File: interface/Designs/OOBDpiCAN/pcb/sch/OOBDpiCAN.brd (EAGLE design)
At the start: 65 x 56 mm, 73 parts, among them Q1 16MHz, X1 RASPI_BOARD_B+_H

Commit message: add USB-HUB GL850G lbr
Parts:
- added U$14: GL850G-31, pimoroni:TSSOP28
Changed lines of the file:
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@@
 <element name="R6" library="resistor" package="R0603" value="120R" x="-49.53" y="50.8"/>
 <element name="X1" library="raspberrypi_bastelstube_v13" package="RASPI_BOARD_B+HAT" value="RASPI_BOARD_B+_H" x="0" y="0"/>
+<element name="U$14" library="pimoroni" package="TSSOP28" value="GL850G-31" x="-78.74" y="5.08"/>
 </elements>
 <signals>

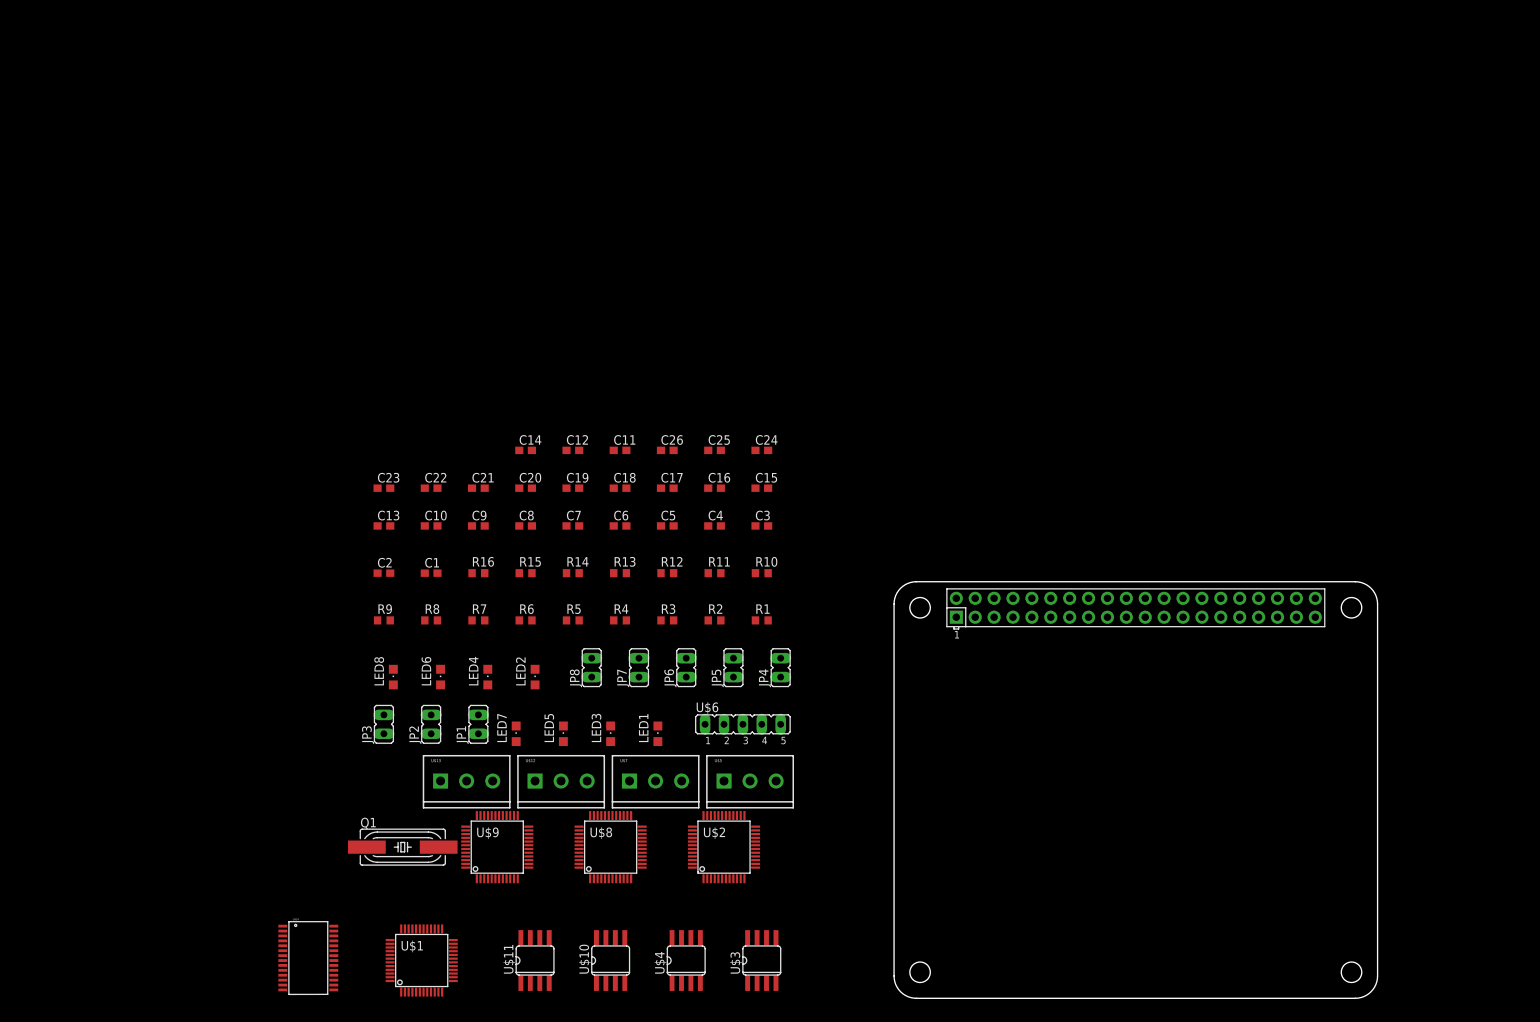
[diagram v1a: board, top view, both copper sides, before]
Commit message: 4Port USB Hub GL850G connected add ISO1050 alternative CAN interfaces
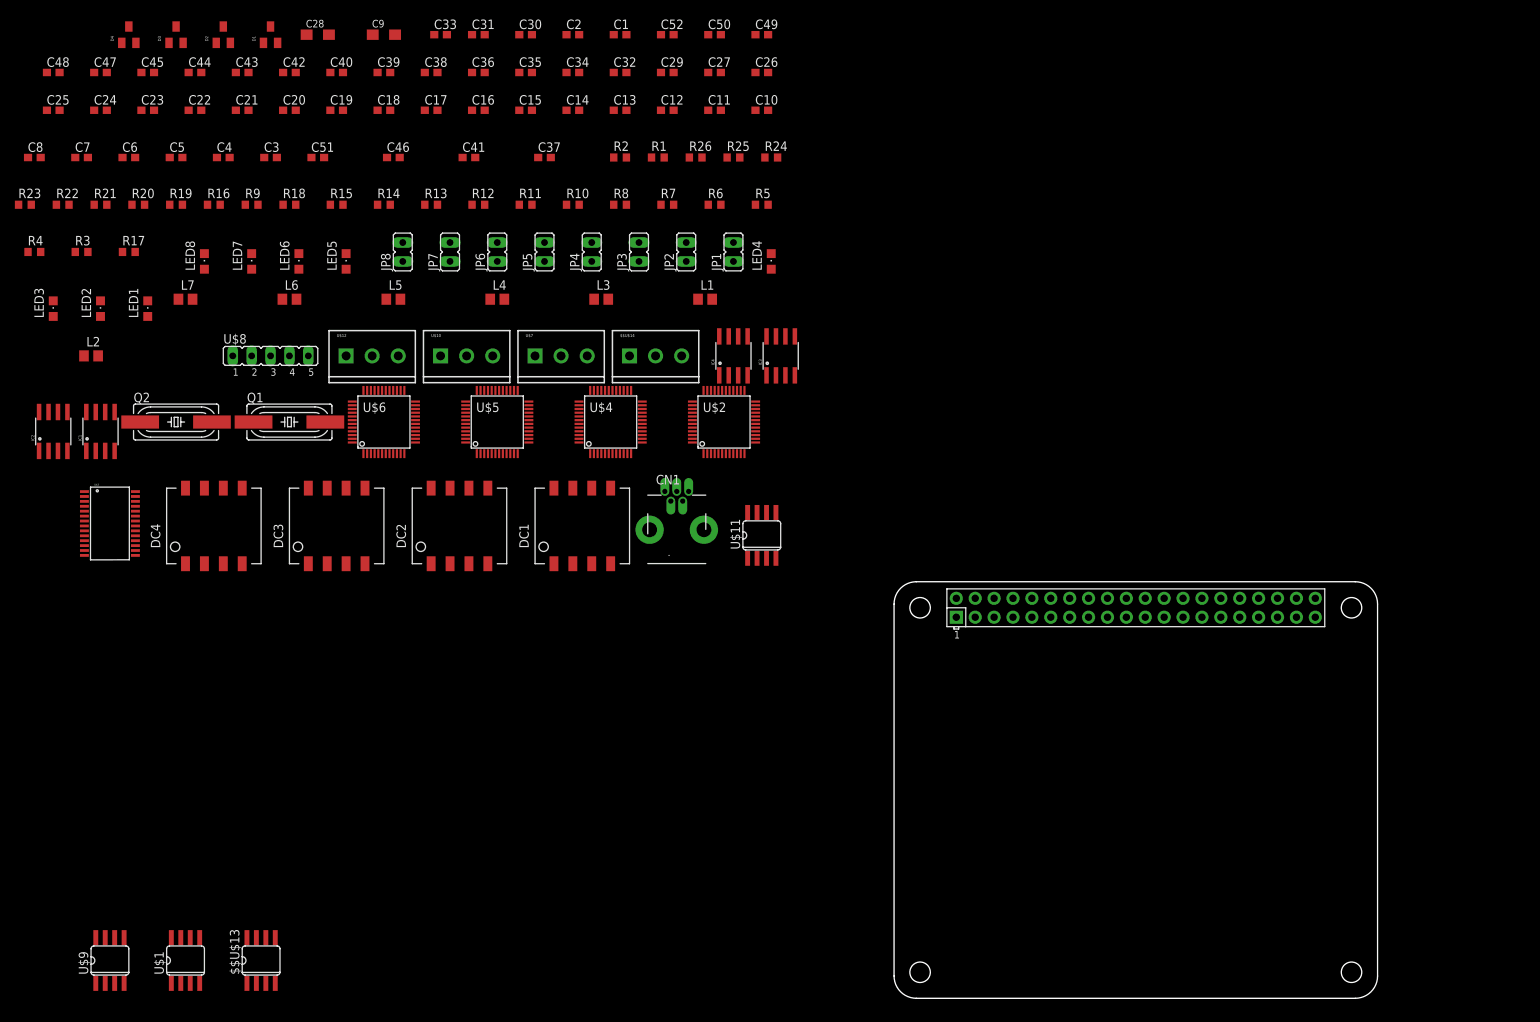
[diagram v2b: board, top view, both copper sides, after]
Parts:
- removed U$13: (no value), SparkFun-Connectors:SCREWTERMINAL-3.5MM-3
- removed U$14: GL850G-31, pimoroni:TSSOP28
- added $$U$13: MCP2551SO8, can:SO08
- added $$U$14: (no value), SparkFun-Connectors:SCREWTERMINAL-3.5MM-3
- added C27, C29, C32, C34, C35, C36, C38, C39, C40, C42, C43, C44, C45, C47, C48, C49, C50, C52: 100nF, resistor:C0603
- added C28: 22uF/6.3V, rcl:SMC_A
- added C30, C31: 18pF, resistor:C0603
- added C33: 1uF, resistor:C0603
- added C37, C41, C46, C51: NA(10nF), resistor:C0603
- added CN1: (no value), adafruit:USB-MINIB-THM-MOLEX
- added D1, D2, D3, D4: PESD1CAN, Industrialberry:SOT23
- added DC1, DC2, DC3, DC4: (no value), Industrialberry:R1SE
- added IC1, IC2, IC3, IC4: (no value), Industrialberry:SO-08
- added L1, L3, L4, L5, L6, L7: 2508056017Y2, rcl:L0805
- added L2: NA(2508056017Y2), rcl:L0805
- added Q2: 16MHz, crystal:SM49
- added R17: NA(47k), resistor:R0603
- added R18: 680R, resistor:R0603
- added R19: 10k, resistor:R0603
- added R20, R21, R22, R23, R24, R25, R26: 60R, resistor:R0603
- C1, C2: value 100nF -> 33pF
- C11, C12, C14: value 18pF -> 100nF
- C9: value 100nF -> 22uF/6.3V; device resistor:C0603 -> rcl:SMC_A
- LED2, LED4: value green -> yellow
- LED5, LED7: value yellow -> green
- Q1: value 16MHz -> 12MHz
- R1, R2: value 510R -> 10k
- R11, R3, R4: value 120R -> 510R
- R16: value 120R -> 10k
- R9: value 510R -> 60R
- U$1, U$9: value STM32F042CT -> MCP2551SO8; device micro-stm_v3:LQFP48 -> can:SO08
- U$10: value MCP2551SO8 -> (none); device can:SO08 -> SparkFun-Connectors:SCREWTERMINAL-3.5MM-3
- U$3: value MCP2551SO8 -> GL850G-31; device can:SO08 -> pimoroni:TSSOP28
- U$4: value MCP2551SO8 -> STM32F042CT; device can:SO08 -> micro-stm_v3:LQFP48
- U$5: value (none) -> STM32F042CT; device SparkFun-Connectors:SCREWTERMINAL-3.5MM-3 -> micro-stm_v3:LQFP48
- U$6: value (none) -> STM32F042CT; device jumper:JP5 -> micro-stm_v3:LQFP48
- U$8: value STM32F042CT -> (none); device micro-stm_v3:LQFP48 -> jumper:JP5
- moved U$3 105.3 mm to (-105.4, 63.5)
- moved C24 100.0 mm to (-106.7, 119.4)
- moved C25 100.0 mm to (-113.0, 119.4)
- moved LED3 94.2 mm to (-113.0, 92.7)
- moved R3 93.0 mm to (-109.2, 100.3)
- moved R4 93.0 mm to (-115.6, 100.3)
- moved LED1 89.3 mm to (-100.3, 92.7)
- moved U$10 84.4 mm to (-61.0, 86.4)
- moved U$8 83.1 mm to (-90.2, 85.1)
- moved C4 82.6 mm to (-90.2, 113.0)
- moved C6 82.6 mm to (-102.9, 113.0)
- moved C3 82.5 mm to (-83.8, 113.0)
- moved C5 82.5 mm to (-96.5, 113.0)
- moved C7 82.5 mm to (-109.2, 113.0)
- moved C8 82.5 mm to (-115.6, 113.0)
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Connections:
- net MC0_2 renamed MCO_0
- removed net N$1: U$10.4, U$8.45
- removed net N$5: U$10.1, U$8.46
- removed net N$9 (its old number): LED6.C, R12.2
- removed net NRST3: U$2.7
- removed net SWCLK2: U$1.37, U$6.2
- removed net SWCLK3: U$2.37
- removed net SWDIO2: U$1.34, U$6.4
- removed net SWDIO3: U$2.34
- removed net USB0_DM1: U$9.32
- removed net USB0_DM2: U$1.32
- removed net USB0_DM3: U$2.32
- removed net USB0_DP1: U$9.33
- removed net USB0_DP2: U$1.33
- removed net USB0_DP3: U$2.33
- new net CAN1-H: D1.2, IC1.7, R20.1, U$1.7, U$7.2
- new net CAN1-L: D1.1, IC1.6, JP3.2, U$1.6, U$7.1
- new net CAN2-H: D3.2, IC3.7, R23.1, U$11.7, U$12.2
- new net CAN2-L: D3.1, IC3.6, JP7.2, U$11.6, U$12.1
- new net CAN3-H: $$U$13.7, $$U$14.2, D4.2, IC4.7, R25.1
- new net CAN3-L: $$U$13.6, $$U$14.1, D4.1, IC4.6, JP8.2
- new net N$17: LED4.C, R14.2
- new net N$2: C1.1, Q1.2, U$3.7
- new net N$3: C2.1, Q1.1, U$3.6
- new net N$33: C6.1, C9.+, L1.2, R1.2, R2.2, U$3.16, U$3.24
- new net N$34: R2.1, U$3.18
- new net N$35: R1.1, U$3.17
- new net N$36: C33.1, R16.2, R17.2, U$3.13
- new net N$37: CN1.D+, U$3.26
- new net N$38: CN1.D-, U$3.25
- new net N$39: C3.1, C4.1, C5.1, L1.1, U$3.1, U$3.10, U$3.5
- new net N$40: R18.2, U$3.4
- new net N$41: CN1.GND, L3.2
- new net N$42: CN1.VBUS, L2.2
- new net N$43: C34.1, DC1.P$2, L4.2
- new net N$44: CN1.ID, R19.2
- new net N$45: C35.1, C35.2, DC1.P$5, IC1.8
- new net N$46: IC2.3, U$2.46, U$9.1
- new net N$47: DC1.P$4, IC1.5
- new net N$48: JP6.1, R22.1
- new net N$49: C37.1, R20.2, R9.2
- new net N$50: C39.1, DC2.P$2, L5.2
- new net N$51: C38.1, C38.2, DC2.P$5, IC2.8
- new net N$52: DC2.P$4, IC2.5
- new net N$53: C41.1, R21.2, R22.2
- new net N$54: $$U$13.1, IC4.3, U$6.46
- new net N$56: IC3.2, U$11.4, U$5.45
- new net N$57: IC3.3, U$11.1, U$5.46
- new net N$59: JP8.1, R26.1
- new net N$60: C49.1, DC4.P$2, L7.2
- new net N$61: C48.1, C48.2, DC4.P$5, IC4.8
- new net N$62: DC4.P$4, IC4.5
- new net N$63: C51.1, R25.2, R26.2
- new net USB1_DM: U$3.2, U$4.32
- new net USB1_DP: U$3.3, U$4.33
- new net USB2_DM: U$3.8, U$5.32
- new net USB2_DP: U$3.9, U$5.33
- new net USB3_DM: U$3.11, U$6.32
- new net USB3_DP: U$3.12, U$6.33
- net +3V3: now also C11.1, C12.1, C13.1, C14.1, C25.1, C26.1, C27.1, C29.1, JP4.1, U$4.1, U$4.24, U$4.36, U$4.48, U$4.9, U$5.1, U$5.24, U$5.36, U$5.48, U$5.9, U$6.24, U$6.36, U$6.48, U$6.9; no longer C1.1, C18.1, C2.1, C3.1, C4.1, C5.1, C6.1, C9.1, JP6.1, U$1.1, U$1.24, U$1.36, U$1.48, U$1.9, U$8.24, U$8.36, U$8.48, U$8.9, U$9.1, U$9.24, U$9.36, U$9.48, U$9.9
- net +5V: now also $$U$13.3, C18.1, C28.+, C32.1, C36.1, C40.1, C42.1, C45.1, C47.1, C50.1, C52.1, IC1.1, IC2.1, IC3.1, IC4.1, L2.1, L4.1, L5.1, L6.1, L7.1, R16.1, U$1.3, U$3.23, U$9.3; no longer C13.1, C14.1, C25.1, C26.1, U$10.3, U$3.3, U$4.3
- net BOOT0: now also JP4.2, R11.2, R3.2, R4.2, U$4.44, U$5.44, U$6.44; no longer JP6.2, R1.2, R2.2, R9.2, U$1.44, U$8.44, U$9.44
- net CAN0-H: now also D2.2, IC2.7, R21.1, U$10.2, U$9.7; no longer R15.2, R16.2, R7.2, R8.2, U$10.7, U$11.7, U$12.2, U$13.2, U$3.7, U$4.7, U$5.2, U$7.2
- net CAN0-L: now also D2.1, IC2.6, JP6.2, U$10.1, U$9.6; no longer JP3.2, JP4.2, JP7.2, JP8.2, U$10.6, U$11.6, U$12.1, U$13.1, U$3.6, U$4.6, U$5.1, U$7.1
- net GND: now also $$U$13.2, $$U$13.8, $$U$14.3, C27.2, C28.-, C29.2, C30.2, C31.2, C32.2, C33.2, C34.2, C36.2, C37.2, C39.2, C40.2, C41.2, C42.2, C44.2, C45.2, C46.2, C47.2, C49.2, C50.2, C51.2, C52.2, C9.-, D1.3, D2.3, D3.3, D4.3, DC1.P$1, DC2.P$1, DC3.P$1, DC4.P$1, IC1.4, IC2.4, IC3.4, IC4.4, L3.1, R15.1, R17.1, R18.1, R19.1, R7.1, R8.1, U$1.2, U$10.3, U$3.14, U$3.15, U$4.23, U$4.35, U$4.47, U$5.23, U$5.35, U$5.47, U$5.8, U$6.23, U$6.35, U$6.47, U$6.8, U$8.3, U$9.2; no longer C9.2, R1.1, R2.1, R9.1, U$1.23, U$1.35, U$1.47, U$10.2, U$10.8, U$13.3, U$3.2, U$3.8, U$4.2, U$5.3, U$6.3, U$8.23, U$8.35, U$8.47, U$8.8, U$9.23, U$9.35, U$9.47
- net MC0_1: now also U$4.29, U$5.5; no longer U$8.5
- net MCO_1: now also U$4.5; no longer U$1.29, U$2.5
- net MCO_2: now also U$5.29, U$6.5; no longer U$8.29, U$9.5
- net N$10: now also C31.1, Q2.2, U$2.6; no longer C12.1, Q1.2, U$1.6
- net N$11: now also C30.1, Q2.1, U$2.5; no longer C11.1, Q1.1, U$1.5
- net N$12: now also C44.1, DC3.P$2, L6.2; no longer U$11.4, U$9.45
- net N$13: now also C43.1, C43.2, DC3.P$5, IC3.8; no longer U$11.1, U$9.46
- net N$14: now also DC3.P$4, IC3.5; no longer JP8.1, R16.1
- net N$15: now also LED4.A, U$6.19; no longer LED7.A, U$9.19
- net N$16: now also U$6.18; no longer U$9.18
- net N$18: now also R15.2; no longer R14.2
- net N$19: now also IC2.2, U$2.45, U$9.4; no longer U$1.45, U$3.4
- net N$20: now also C46.1, R23.2, R24.2; no longer U$1.46, U$3.1
- net N$21: now also $$U$13.4, IC4.2, U$6.45; no longer JP3.1, R7.1
- net N$22: now also U$2.19; no longer U$1.19
- net N$23: now also LED5.A, U$2.18; no longer LED2.A, U$1.18
- net N$24: now also R5.2; no longer R3.2
- net N$25: now also LED5.C, R6.2; no longer LED2.C, R4.2
- net N$26: now also IC1.2, U$1.4, U$4.45; no longer U$2.45, U$4.4
- net N$27: now also IC1.3, U$1.1, U$4.46; no longer U$2.46, U$4.1
- net N$28: now also JP3.1, R9.1; no longer JP4.1, R8.1
- net N$29: now also LED2.A, U$4.19; no longer LED3.A, U$2.19
- net N$30: now also LED6.A, U$4.18; no longer LED4.A, U$2.18
- net N$31: now also LED2.C, R7.2; no longer LED3.C, R5.2
- net N$32: now also LED6.C, R8.2; no longer LED4.C, R6.2
- net N$4: now also LED3.A, U$5.19; no longer LED5.A, U$8.19
- net N$6: now also R24.1; no longer R15.1
- net N$7: now also LED7.A, U$5.18; no longer LED6.A, U$8.18
- net N$8: now also LED3.C, R12.2; no longer LED5.C, R11.2
- net NRST: now also U$4.7, U$5.7, U$8.5; no longer U$8.7
- net NRST1: now also U$6.7; no longer U$9.7
- net NRST2: now also U$2.7; no longer U$1.7, U$6.5
- net PA4: now also U$4.14, U$5.14, U$6.14; no longer U$1.14, U$8.14, U$9.14
- net PA5: now also U$4.15, U$5.15, U$6.15; no longer U$1.15, U$8.15, U$9.15
- net PF1-OSC_OUT: now also U$4.6, U$5.6, U$6.6; no longer U$2.6, U$8.6, U$9.6
- net SWCLK: now also U$2.37, U$4.37, U$5.37, U$8.2; no longer U$8.37
- net SWCLK1: now also U$6.37; no longer U$9.37
- net SWDIO: now also U$2.34, U$4.34, U$5.34, U$8.4; no longer U$8.34
- net SWDIO1: now also U$6.34; no longer U$9.34
- net USB0_DM: now also U$2.32, U$3.27; no longer U$8.32
- net USB0_DP: now also U$2.33, U$3.28; no longer U$8.33

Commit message: - fix ERC (Pwr supply) issues due to faulty GL850G symbol - exchange ISO1050 against ADMU3053 and limit to a max of 2x galvanic isolated CAN-Interface due to size of PCB
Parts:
- removed C47, C48, C49, C52: 100nF, resistor:C0603
- removed DC1, DC2, DC3, DC4: (no value), Industrialberry:R1SE
- removed IC2, IC3, IC4: (no value), Industrialberry:SO-08
- removed L4, L5, L6, L7: 2508056017Y2, rcl:L0805
- removed X1: RASPI_BOARD_B+_H, raspberrypi_bastelstube_v13:RASPI_BOARD_B+HAT
- added BAT2: (no value), SparkFun:BATTCON_12MM_PTH
- added C53: 1uF, rcl:C0603
- added C54: 100nF, rcl:C0603
- added C55: 10n, rcl:C0603K
- added C56, C58: 100n, rcl:C0603K
- added C57, C61: 10u, rcl:C0805K
- added C59, C62: 100n, rcl:C0805K
- added C60: 10n, rcl:C0805K
- added IC5: DS3231, DS3231_industrialberry:SOIC-16W
- added IC6: EEPROM24, FLYFISH:SOIC8
- added IC7: ADM3053M, ADM3053:SO20W
- added JP10: (no value), SparkFun:SJ_2S-NO
- added JP9: (no value), MirkoSmartSpaceSolutions:MA03-1
- added R27, R28, R29, R30: 10k, rcl:R0603
- added R31, R32: 8.2k, rcl:R0603
- added R33: (no value), rcl:0204/7
- added RPI1: (no value), Connector_B+:CONNECTOR_B+_SMT_HAT
- added SJ2: SOLDERJUMPERTRACE, SparkFun:SJ_2S-TRACE
- C34: value 100nF -> 10n; device resistor:C0603 -> rcl:C0603K
- C35, C38: value 100nF -> 100n; device resistor:C0603 -> rcl:C0603K
- C36, C43: value 100nF -> 10u; device resistor:C0603 -> rcl:C0805K
- C39, C44: value 100nF -> 100n; device resistor:C0603 -> rcl:C0805K
- C42: value 100nF -> 10n; device resistor:C0603 -> rcl:C0805K
- C46: value NA(10nF) -> NA(47nF)
- IC1: value (none) -> ADM3053M; device Industrialberry:SO-08 -> ADM3053:SO20W
- moved U$1 144.0 mm to (48.3, 16.5)
- moved Q1 139.2 mm to (53.3, 41.9)
- moved IC1 134.0 mm to (14.0, 17.8)
- moved U$3 133.8 mm to (26.7, 41.9)
- moved U$9 130.9 mm to (25.4, 10.2)
- moved $$U$13 129.6 mm to (44.5, 10.2)
- moved $$U$14 116.7 mm to (47.0, 3.81)
- moved U$10 116.7 mm to (21.6, 3.81)
- moved U$12 116.7 mm to (8.89, 3.81)
- moved U$7 116.7 mm to (34.3, 3.81)
- moved Q2 114.5 mm to (12.7, 43.2)
- moved U$6 94.4 mm to (14.0, 31.8)
- moved U$5 93.9 mm to (27.9, 30.5)
- moved U$4 89.5 mm to (38.1, 30.5)
- moved U$2 85.2 mm to (48.3, 30.5)
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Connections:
- removed net 3V3: X1.1
- removed net 5V0: X1.2
- removed net N$14: DC3.P$4, IC3.5
- removed net N$19: IC2.2, U$2.45, U$9.4
- removed net N$26: IC1.2, U$1.4, U$4.45
- removed net N$27: IC1.3, U$1.1, U$4.46
- removed net N$43: C34.1, DC1.P$2, L4.2
- removed net N$45: C35.1, C35.2, DC1.P$5, IC1.8
- removed net N$46: IC2.3, U$2.46, U$9.1
- removed net N$47: DC1.P$4, IC1.5
- removed net N$50: C39.1, DC2.P$2, L5.2
- removed net N$51: C38.1, C38.2, DC2.P$5, IC2.8
- removed net N$52: DC2.P$4, IC2.5
- removed net N$60: C49.1, DC4.P$2, L7.2
- removed net N$61: C48.1, C48.2, DC4.P$5, IC4.8
- removed net N$62: DC4.P$4, IC4.5
- removed net PA4: U$2.14, U$4.14, U$5.14, U$6.14
- removed net PA5: U$2.15, U$4.15, U$5.15, U$6.15
- removed net PF1-OSC_OUT: U$4.6, U$5.6, U$6.6
- new net CAN0_RXD: IC7.4, U$2.45, U$9.4
- new net CAN0_TXD: IC7.5, U$2.46, U$9.1
- new net CAN1_RXD: IC1.4, U$1.4, U$4.45
- new net CAN1_TXD: IC1.5, U$1.1, U$4.46
- new net GNDA: C39.2, C42.2, C43.2, C44.2, C59.2, C60.2, C61.2, C62.2, IC1.11, IC1.13, IC1.16, IC1.20, IC7.11, IC7.13, IC7.16, IC7.20, R31.1, R32.1
- new net GPIO17: RPI1.11
- new net ID_SC: IC6.6, R28.2, RPI1.28
- new net ID_SD: IC6.5, R29.2, RPI1.27
- new net INT-: IC5.3, JP10.2, R27.1
- new net N$1: IC7.18, R31.2
- new net N$5: IC6.7, R30.2, SJ2.2
- new net N$55: JP10.1
- new net N$65: C59.1, C60.1, C61.1, C62.1, IC7.12, IC7.19
- new net RXD: JP9.2, RPI1.10
- new net SCL: IC5.16, RPI1.5
- new net SDA: IC5.15, RPI1.3
- new net TXD: JP9.3, RPI1.8
- new net VBAT: BAT2.VCC@1, IC5.14
- net +3V3: now also C34.1, C35.1, C53.2, C55.1, C56.1, IC1.6, IC5.2, IC7.6, R27.2, RPI1.1, RPI1.17
- net +5V: now also C38.1, C54.2, C57.1, C58.1, IC1.8, IC6.8, IC7.8, R28.1, R29.1, R30.1, RPI1.2, RPI1.4; no longer C42.1, C47.1, C52.1, IC1.1, IC2.1, IC3.1, IC4.1, L4.1, L5.1, L6.1, L7.1
- net CAN0-H: now also IC7.17; no longer IC2.7
- net CAN0-L: now also IC7.15; no longer IC2.6
- net CAN1-H: now also IC1.17; no longer IC1.7
- net CAN1-L: now also IC1.15; no longer IC1.6
- net CAN2-H: no longer IC3.7
- net CAN2-L: no longer IC3.6
- net CAN3-H: no longer IC4.7
- net CAN3-L: no longer IC4.6
- net GND: now also BAT2.GND, C35.2, C38.2, C53.1, C54.1, C55.2, C56.2, C57.2, C58.2, IC1.1, IC1.10, IC1.3, IC1.7, IC1.9, IC5.10, IC5.11, IC5.12, IC5.13, IC5.5, IC5.6, IC5.7, IC5.8, IC5.9, IC6.1, IC6.2, IC6.3, IC6.4, IC7.1, IC7.10, IC7.3, IC7.7, IC7.9, JP9.1, RPI1.14, RPI1.20, RPI1.25, RPI1.30, RPI1.34, RPI1.39, RPI1.6, RPI1.9, SJ2.1; no longer C39.2, C42.2, C44.2, C47.2, C49.2, C52.2, DC1.P$1, DC2.P$1, DC3.P$1, DC4.P$1, IC1.4, IC2.4, IC3.4, IC4.4, X1.6
- net N$12: now also IC1.18, R32.2; no longer C44.1, DC3.P$2, L6.2
- net N$13: now also C39.1, C42.1, C44.1, IC1.12, IC1.19; no longer C43.2, DC3.P$5, IC3.8
- net N$21: no longer IC4.2
- net N$54: no longer IC4.3
- net N$56: no longer IC3.2
- net N$57: no longer IC3.3
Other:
- board size 65 x 56 mm -> 65.1 x 57.3 mm

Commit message: exchange X-references from supply2 library to X-Ref symbols
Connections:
- removed net N$55: JP10.1
- removed net NRST2: U$2.7
- net GPIO17: now also JP10.1
- net NRST: now also U$2.7
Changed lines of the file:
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@@
 <wire x1="-17.145" y1="59.1566" x2="7.57" y2="54.77" width="0" layer="19" extent="1-16"/>
-</signal>
-<signal name="NRST2">
-<contactref element="U$2" pad="7"/>
 </signal>
 <signal name="N$10">
@@
 <contactref element="U$8" pad="5"/>
 <contactref element="U$5" pad="7"/>
+<contactref element="U$2" pad="7"/>
+<wire x1="38.35" y1="26.23" x2="48.51" y2="26.23" width="0" layer="19" extent="1-1"/>
 <wire x1="28.19" y1="26.23" x2="38.35" y2="26.23" width="0" layer="19" extent="1-1"/>
 <wire x1="-71.12" y1="12.7" x2="28.19" y2="26.23" width="0" layer="19" extent="1-1"/>
@@
 <wire x1="17.73" y1="54.77" x2="20.32" y2="71.12" width="0" layer="19" extent="16-16"/>
 </signal>
-<signal name="N$55">
-<contactref element="JP10" pad="1"/>
-</signal>
 <signal name="INT-">
 <contactref element="JP10" pad="2"/>
@@
 <signal name="GPIO17">
 <contactref element="RPI1" pad="11"/>
+<contactref element="JP10" pad="1"/>
+<wire x1="5.9" y1="59.69" x2="20.27" y2="49.37" width="0" layer="19" extent="1-16"/>
 </signal>
 <signal name="CAN0_TXD">

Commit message: start placing parts
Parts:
- added R34, R35, R36: 0R, rcl:0207/10
- R33: value (none) -> 0R; device rcl:0204/7 -> rcl:0207/10
- moved R20 122.2 mm to (25.4, 6.99)
- moved D1 119.7 mm to (33.7, 8.26)
- moved R22 117.2 mm to (10.2, 6.99)
- moved R21 113.1 mm to (11.4, 8.89), turned to 180 degrees
- moved D2 111.6 mm to (18.4, 8.26), turned to 270 degrees
- moved R9 106.8 mm to (25.4, 9.53)
- moved JP9 97.9 mm to (-61.0, 16.5)
- moved U$11 89.9 mm to (58.4, 14.6), flipped to the bottom, turned to 180 degrees
- moved R33 81.5 mm to (13.3, 17.8), turned to 270 degrees
- moved C58 77.4 mm to (26.0, 26.7), turned to 180 degrees
- moved C57 75.3 mm to (26.0, 28.6), turned to 180 degrees
- moved C37 75.0 mm to (29.2, 8.89)
- moved C41 71.6 mm to (14.6, 7.62)
- moved C36 71.3 mm to (10.2, 28.6)
- moved C38 71.2 mm to (10.2, 26.7)
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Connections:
- new net N$14: R33.1, U$9.6
- new net N$19: R34.1, U$9.7
- new net N$26: R36.1, U$1.7
- new net N$27: R35.1, U$1.6
- net CAN0-H: now also R34.2; no longer U$9.7
- net CAN0-L: now also R33.2; no longer U$9.6
- net CAN1-H: now also R36.2; no longer U$1.7
- net CAN1-L: now also R35.2; no longer U$1.6
